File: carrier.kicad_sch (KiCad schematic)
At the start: 65 parts, among them J1 Conn_02x06_Odd_Even, J10 Conn_01x02, J11 Conn_01x02, J12 AudioJack3_SwitchTR, J13 Conn_02x06_Odd_Even, J2 Conn_01x26, J3 Conn_01x26, J4 TYPE-C-31-M-12, J5 Conn_01x02, J6 Conn_01x02, J7 Conn_01x02, J8 Conn_01x02, J9 Conn_01x02, SW1 SW_Push, SW2 SW_Push, SW3 SW_Push, SW4 SW_Push, SW5 SW_Push, SW6 SW_Push, U1 CARAVEL, U2 W25Q128JVS, U3 LP5907MFX-3.3, U4 LP5907MFX-1.8, U5 LP5907MFX-1.8, U6 LP5907MFX-3.3, U8 OPA340NA, U9 OPA340NA, X1 SG-5032CAN

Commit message: schematics: Cleanup schematics
* Divide the subcircuits using grid
* Annotate symbol name to ESDS312DBVR

Signed-off-by: Vedant Paranjape <22630228+VedantParanjape@users.noreply.github.com>
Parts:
- gave numbers to parts that had none: 1
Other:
- moved on the sheet: C1, C18, C19, C2, C20, C21, C3, C4, C5, C6, C7, C8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

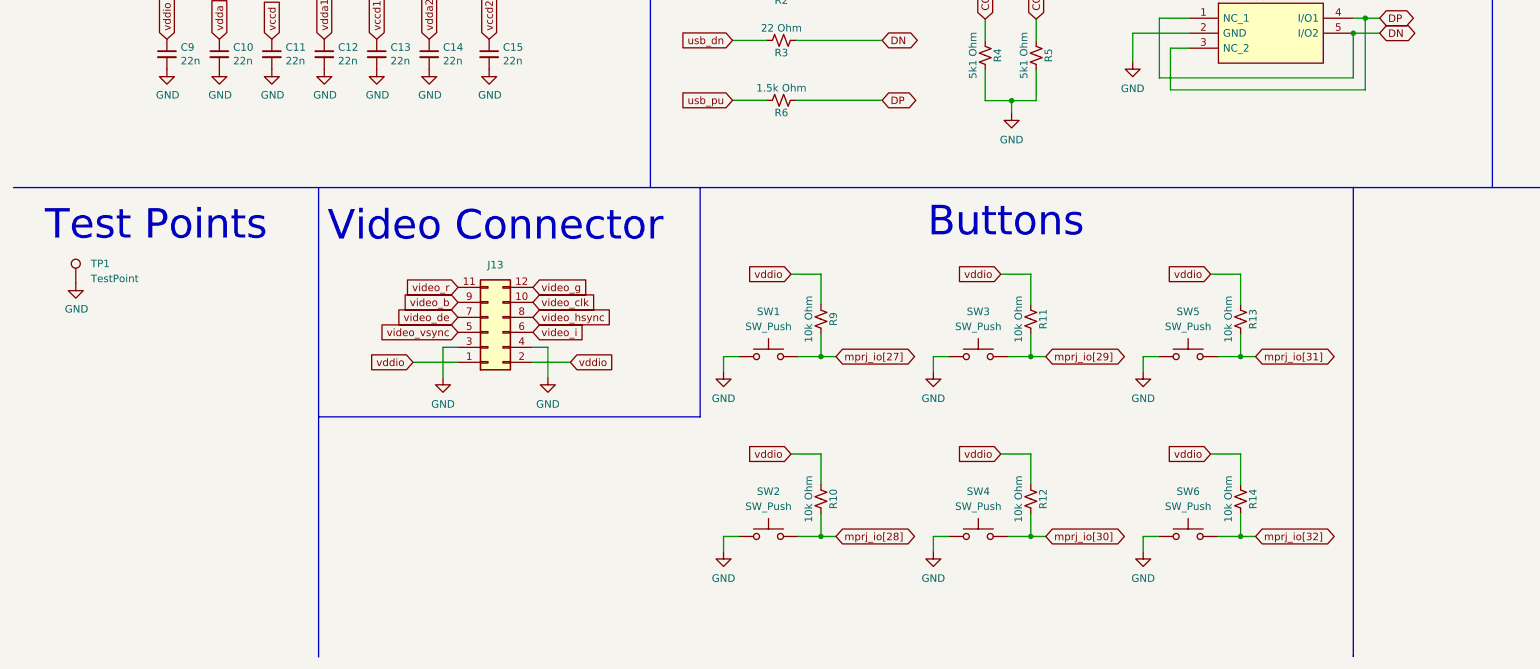
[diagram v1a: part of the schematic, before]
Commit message: schematics: Added ESD Protection for buttons
Add ESDS312DBVR chip to the input GPIOs connected to the buttons.

Signed-off-by: Vedant Paranjape <22630228+VedantParanjape@users.noreply.github.com>
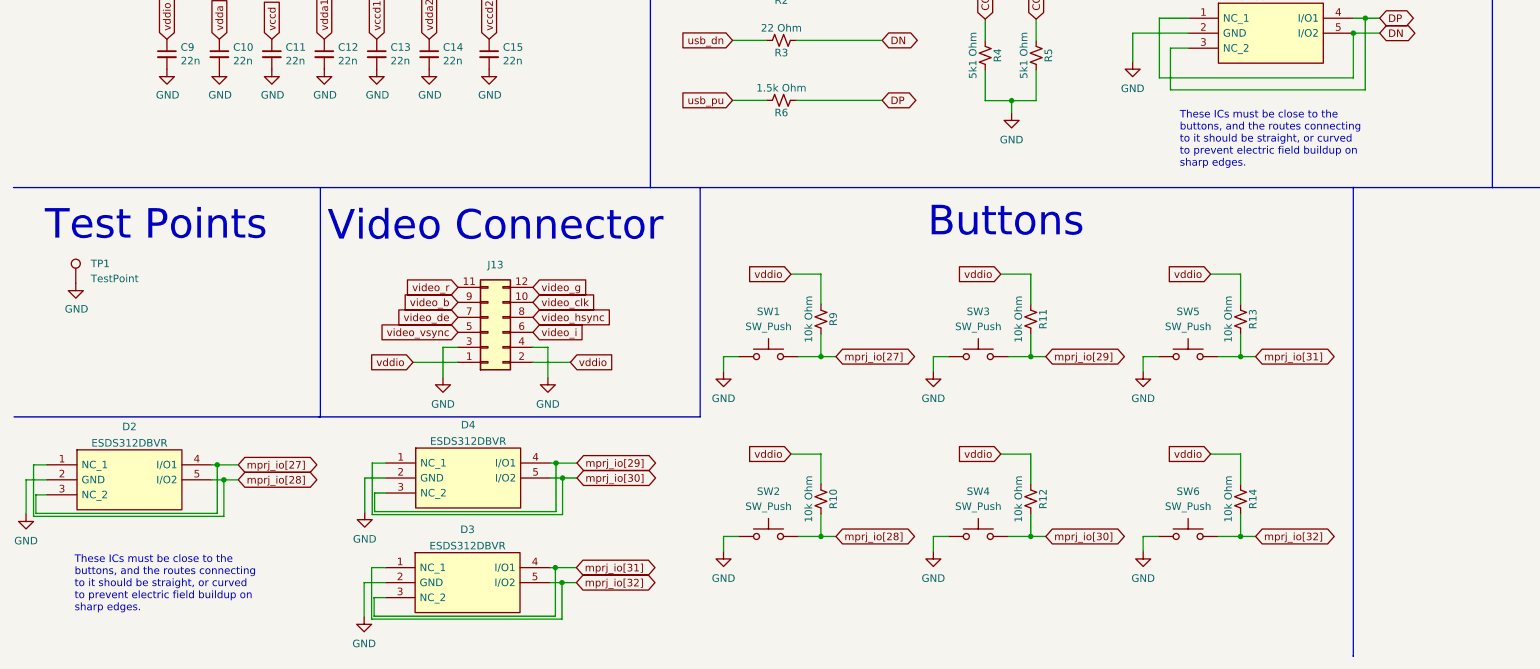
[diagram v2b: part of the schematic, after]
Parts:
- added D2, D3, D4: ESDS312DBVR, SOT95P280X145-5N, symbol ESDS312DBVR:ESDS312DBVR
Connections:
- net GND: now also D2.2 (GND), D3.2 (GND), D4.2 (GND)
- net mprj_io[27]: now also D2.3 (NC_2), D2.4 (I/O1)
- net mprj_io[28]: now also D2.1 (NC_1), D2.5 (I/O2)
- net mprj_io[29]: now also D4.3 (NC_2), D4.4 (I/O1)
- net mprj_io[30]: now also D4.1 (NC_1), D4.5 (I/O2)
- net mprj_io[31]: now also D3.3 (NC_2), D3.4 (I/O1)
- net mprj_io[32]: now also D3.1 (NC_1), D3.5 (I/O2)
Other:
- note added: "These ICs must be close to the buttons, and the routes connecting to it should be straight, or curved to prevent electric field buildup on sharp edges."

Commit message: Switch KiCAD standard SOT-23-5 footprint
No need to reinvent the wheel.
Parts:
- D1, D2, D3, D4: footprint SOT95P280X145-5N -> Package_TO_SOT_SMD:SOT-23-5
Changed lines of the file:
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@@
     (property "Reference" "D2" (id 0) (at 31.75 245.817 0))
     (property "Value" "ESDS312DBVR" (id 1) (at 31.75 248.5921 0))
-    (property "Footprint" "SOT95P280X145-5N" (id 2) (at 41.91 249.7328 0)
+    (property "Footprint" "Package_TO_SOT_SMD:SOT-23-5" (id 2) (at 41.91 249.7328 0)
       (effects (font (size 1.27 1.27)) (justify left) hide)
     )
@@
     (property "Reference" "D3" (id 0) (at 89.0524 263.2414 0))
     (property "Value" "ESDS312DBVR" (id 1) (at 89.0524 266.0165 0))
-    (property "Footprint" "SOT95P280X145-5N" (id 2) (at 99.2124 267.1572 0)
+    (property "Footprint" "Package_TO_SOT_SMD:SOT-23-5" (id 2) (at 99.2124 267.1572 0)
       (effects (font (size 1.27 1.27)) (justify left) hide)
     )
@@
     (property "Reference" "D4" (id 0) (at 89.154 245.5122 0))
     (property "Value" "ESDS312DBVR" (id 1) (at 89.154 248.2873 0))
-    (property "Footprint" "SOT95P280X145-5N" (id 2) (at 99.314 249.428 0)
+    (property "Footprint" "Package_TO_SOT_SMD:SOT-23-5" (id 2) (at 99.314 249.428 0)
       (effects (font (size 1.27 1.27)) (justify left) hide)
     )
@@
     (property "Reference" "D1" (id 0) (at 225.1964 170.125 0))
     (property "Value" "ESDS312DBVR" (id 1) (at 225.1964 172.9001 0))
-    (property "Footprint" "SOT95P280X145-5N" (id 2) (at 235.3564 174.0408 0)
+    (property "Footprint" "Package_TO_SOT_SMD:SOT-23-5" (id 2) (at 235.3564 174.0408 0)
       (effects (font (size 1.27 1.27)) (justify left) hide)
     )
@@
     )
     (path "/46cd44db-36fc-4682-b156-bf1dfcd88f9c"
-      (reference "D1") (unit 1) (value "ESDS312DBVR") (footprint "SOT95P280X145-5N")
+      (reference "D1") (unit 1) (value "ESDS312DBVR") (footprint "Package_TO_SOT_SMD:SOT-23-5")
     )
     (path "/f66d4703-abae-4705-a5e8-c7b39745ba49"
-      (reference "D2") (unit 1) (value "ESDS312DBVR") (footprint "SOT95P280X145-5N")
+      (reference "D2") (unit 1) (value "ESDS312DBVR") (footprint "Package_TO_SOT_SMD:SOT-23-5")
     )
     (path "/fbcdfc34-1ed4-43fc-84b1-8c77050ee3cc"
-      (reference "D3") (unit 1) (value "ESDS312DBVR") (footprint "SOT95P280X145-5N")
+      (reference "D3") (unit 1) (value "ESDS312DBVR") (footprint "Package_TO_SOT_SMD:SOT-23-5")
     )
     (path "/baa4bb46-b130-458c-96c1-fa72aa333353"
-      (reference "D4") (unit 1) (value "ESDS312DBVR") (footprint "SOT95P280X145-5N")
+      (reference "D4") (unit 1) (value "ESDS312DBVR") (footprint "Package_TO_SOT_SMD:SOT-23-5")
     )
     (path "/00000000-0000-0000-0000-00005fcd8a9b"

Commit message: schematics: Add subcircuit for RGB LED
* Uses LRTBGVSRU4V2JWA6BBD8S2U27Z20S RGB Led, with common cathode config

Signed-off-by: Vedant Paranjape <22630228+VedantParanjape@users.noreply.github.com>
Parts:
- added LED1: LRTBGVSR-U4V2-JW+A6BB-D8+S2U2-7Z-20-S, LRTBGVSRU4V2JWA6BBD8S2U27Z20S, symbol LRTBGVSR-U4V2-JW+A6BB-D8+S2U2-:LRTBGVSR-U4V2-JW+A6BB-D8+S2U2-7Z-20-S
- added R15, R16, R17: 1k Ohm, Resistor_SMD:R_0402_1005Metric, symbol Device:R_Small_US
- D1, D2, D3, D4: footprint Package_TO_SOT_SMD:SOT-23-5 -> SOT95P280X145-5N
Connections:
- net GND: now also LED1.C1 (CATHODE_TRUE_GREEN), LED1.C2 (CATHODE_RED), LED1.C3 (CATHODE_BLUE)
- net mprj_io[27]: no longer U1.A4 (mprj_io[27])
- net mprj_io[28]: no longer U1.B5 (mprj_io[28])
- net mprj_io[29]: no longer U1.A5 (mprj_io[29])
- new net: LED1.A3 (ANODE_BLUE), R15.1
- new net: LED1.A1 (ANODE_TRUE_GREEN), R17.2
- new net: LED1.A2 (ANODE_RED), R16.2
- new net RGB_LED_B: R15.2, U1.A5 (mprj_io[29])
- new net RGB_LED_G: R17.1, U1.B5 (mprj_io[28])
- new net RGB_LED_R: R16.1, U1.A4 (mprj_io[27])
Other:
- note added: "RGB Led"
